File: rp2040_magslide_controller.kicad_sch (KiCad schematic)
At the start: 45 parts, among them J1 USB_B_Mini, J2 50-00174, J3 Conn_02x05_Odd_Even, J4 Conn_01x20_Female, J5 Conn_01x20_Female, SW2 SW_SPST, U2 AMS1117-3.3, U4 CD74HC4067SM, U5 CD74HC4067SM

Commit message: Inc
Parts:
- added C20: 0.1u, symbol Device:C_Small
- added H1: (no value), symbol Mechanical:MountingHole
- added H2, H3, H4: MountingHole, symbol Mechanical:MountingHole
- C1, C10, C11, C12, C13, C14, C15, C16, C17: value (none) -> 0.1u
- C4, C5: value (none) -> 12p
- C9: value 0.1u -> (none)
- R2: value (none) -> 1K
- R4: value (none) -> 10K
- R8: value (none) -> 27R 0603
- SW1: value (none) -> SW_SPST
- U1: value (none) -> W25Q64JV; footprint (none) -> Package_SON:WSON-8-1EP_6x5mm_P1.27mm_EP3.4x4mm
- U3: value (none) -> RP2040; footprint (none) -> RP2040_minimal:RP2040-QFN-56
- Y1: value (none) -> 12Mhz
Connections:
- net +3V3: now also C11.1, C12.1, C13.1, C14.1, C15.1, C16.1, C17.1, C20.1; no longer C11.2, C12.2, C13.2, C14.2, C15.2, C16.2, C17.2
- net GND: now also C10.2, C11.2, C12.2, C13.2, C14.2, C15.2, C16.2, C17.2, C8.2, C9.2, C20.2; no longer C10.1, C11.1, C12.1, C13.1, C14.1, C15.1, C16.1, C17.1, C8.1, C9.1
- net +1V1: now reaches U3.23 (DVDD), U3.45 (VREG_VOUT), U3.50 (DVDD)
- net +1V1: now also C10.1, C8.1, C9.1; no longer C10.2, C8.2, C9.2
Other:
- note added: "Close to chip"
- moved on the sheet: C2, C3, C6, C7, U2

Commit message: WIP for layout, need new footprint for rp2040 for some reason...
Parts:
- removed J4, J5: Conn_01x20_Female, misc:20_pin_header, symbol Connector:Conn_01x20_Female
- added J4: (no value), symbol Connector_Generic:Conn_02x20_Odd_Even
- C8: value (none) -> 0.1u
- C9: value (none) -> 1u
- H1: value (none) -> MountingHole
- U3: footprint RP2040_minimal:RP2040-QFN-56 -> (none)
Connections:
- net +3V3: now also J4.1 (Pin_1), J4.15 (Pin_15), J4.18 (Pin_18), J4.29 (Pin_29), J4.4 (Pin_4)
- net +5V: now also J4.36 (Pin_36)
- net F00: now also J4.5 (Pin_5)
- net F01: now also J4.7 (Pin_7)
- net F02: now also J4.9 (Pin_9)
- net F03: now also J4.11 (Pin_11)
- net F04: now also J4.13 (Pin_13)
- net F10: now also J4.19 (Pin_19)
- net F11: now also J4.21 (Pin_21)
- net F12: now also J4.23 (Pin_23)
- net F13: now also J4.25 (Pin_25)
- net F14: now also J4.27 (Pin_27)
- net F20: now also J4.33 (Pin_33)
- net F21: now also J4.35 (Pin_35)
- net F22: now also J4.37 (Pin_37)
- net F23: now also J4.39 (Pin_39)
- net F24: now also J4.2 (Pin_2)
- net F30: now also J4.8 (Pin_8)
- net F31: now also J4.10 (Pin_10)
- net F32: now also J4.12 (Pin_12)
- net F33: now also J4.14 (Pin_14)
- net F34: now also J4.16 (Pin_16)
- net F40: now also J4.22 (Pin_22)
- net F41: now also J4.24 (Pin_24)
- net F42: now also J4.26 (Pin_26)
- net F43: now also J4.28 (Pin_28)
- net F44: now also J4.30 (Pin_30)
- net GND: now also J4.17 (Pin_17), J4.20 (Pin_20), J4.3 (Pin_3), J4.31 (Pin_31), J4.38 (Pin_38), J4.6 (Pin_6)
- net extern_scl: now also J4.32 (Pin_32)
- net extern_sda: now also J4.34 (Pin_34)

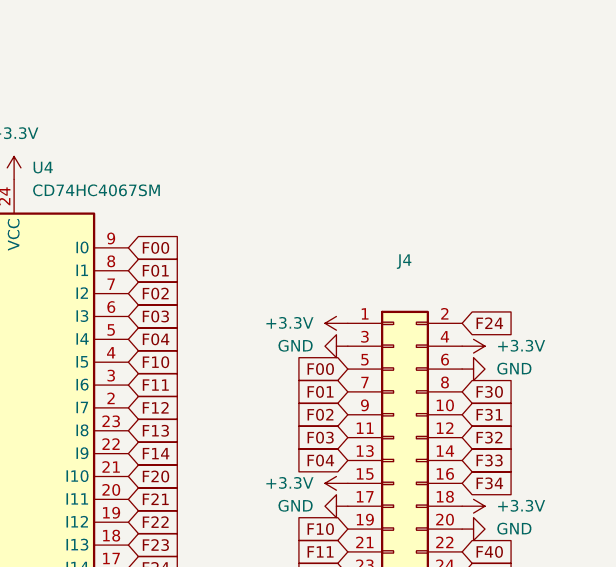
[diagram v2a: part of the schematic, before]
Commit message: Adds SOP8 flash instead
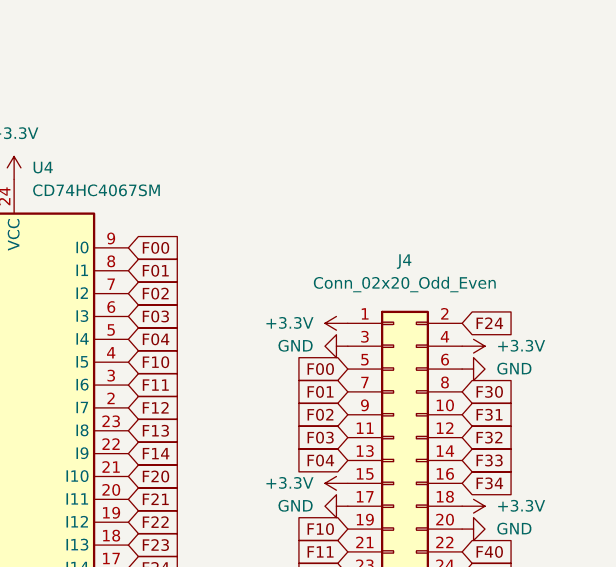
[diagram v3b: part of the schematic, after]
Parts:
- C1, C10, C11, C12, C13, C14, C15, C16, C17, C20, C4, C5, C8: footprint (none) -> Capacitor_SMD:C_0402_1005Metric
- C9: footprint (none) -> Capacitor_SMD:C_0603_1608Metric
- H1, H2, H3, H4: footprint (none) -> MountingHole:MountingHole_3.2mm_M3
- J4: value (none) -> Conn_02x20_Odd_Even; footprint (none) -> Connector_PinSocket_2.54mm:PinSocket_2x20_P2.54mm_Vertical
- R2, R4, R7: footprint (none) -> Resistor_SMD:R_0402_1005Metric
- R8, R9: footprint (none) -> Resistor_SMD:R_0603_1608Metric
- SW1, SW2: footprint (none) -> local:SW_TS-1187A-B-A-B
- U1: footprint Package_SON:WSON-8-1EP_6x5mm_P1.27mm_EP3.4x4mm -> (none)
- U3: footprint (none) -> MCU_RaspberryPi_and_Boards:RP2040-QFN-56
- Y1: footprint (none) -> Crystal:Crystal_SMD_3225-4Pin_3.2x2.5mm
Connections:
- net GND: no longer U1.9 (GND)

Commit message: Inc
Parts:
- removed C18, C19: 100n, Capacitor_SMD:C_0402_1005Metric, symbol Device:C_Small
- removed C2, C6: 4u7, Capacitor_SMD:C_0603_1608Metric, symbol Device:C_Small
- removed C3, C7: 1u, Capacitor_SMD:C_0603_1608Metric, symbol Device:C_Small
- removed H1, H2, H3, H4: MountingHole, MountingHole:MountingHole_3.2mm_M3, symbol Mechanical:MountingHole
- removed J1: USB_B_Mini, Connector_USB:USB_Micro-B_Molex-105017-0001, symbol Connector:USB_B_Mini
- removed J4: Conn_02x20_Odd_Even, Connector_PinSocket_2.54mm:PinSocket_2x20_P2.54mm_Vertical, symbol Connector_Generic:Conn_02x20_Odd_Even
- removed JP1, JP2: SolderJumper_2_Open, Jumper:SolderJumper-2_P1.3mm_Open_TrianglePad1.0x1.5mm, symbol Jumper:SolderJumper_2_Open
- removed R10, R11: 10k, Resistor_SMD:R_0402_1005Metric, symbol Device:R_Small
- removed R2: 1K, Resistor_SMD:R_0402_1005Metric, symbol Device:R_Small
- removed R5, R6: 4.7k, Resistor_SMD:R_0402_1005Metric, symbol Device:R_Small
- removed R8, R9: 27R 0603, Resistor_SMD:R_0603_1608Metric, symbol Device:R_Small
- removed SW1, SW2: SW_SPST, local:SW_TS-1187A-B-A-B, symbol Switch:SW_SPST
- removed U2: AMS1117-3.3, Package_TO_SOT_SMD:SOT-223-3_TabPin2, symbol Regulator_Linear:AMS1117-3.3
- removed U4, U5: CD74HC4067SM, Package_SO:SSOP-24_5.3x8.2mm_P0.65mm, symbol 74xx:CD74HC4067SM
- added C? (x3): 10uF, Capacitor_SMD:C_0603_1608Metric, symbol Device:C_Small
- added C?: 100nF, Capacitor_SMD:C_0603_1608Metric, symbol Device:C_Small
- added J?: Pressure sensor, symbol Connector:Conn_01x02_Female
- added JP? (x3): SolderJumper_2_Open, symbol Jumper:SolderJumper_2_Open
- added R?: 10k, Resistor_SMD:R_0402_1005Metric, symbol Device:R_Small
- added S? (x4): OH49E-S, symbol magslide:OH49E-S
- added U?: AP2112K-3.3, Package_TO_SOT_SMD:SOT-23-5, symbol Regulator_Linear:AP2112K-3.3
- added U?: LIS3DH, Package_LGA:LGA-16_3x3mm_P0.5mm_LayoutBorder3x5y, symbol Sensor_Motion:LIS3DH
- added U?: SGM3157, symbol magslide:SGM3157
- U1: footprint (none) -> Package_SO:SOP-8_5.28x5.23mm_P1.27mm
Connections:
- net +3V3: now also C?.1, C?.1, J?.1 (Pin_1), S?.1 (VCC), S?.1 (VCC), S?.1 (VCC), S?.1 (VCC), U?.5 (VOUT), U?.5 (Vcc)
- net +5V: now also C?.1, C?.1, U?.1 (VIN), U?.3 (EN)
- net GND: now also C?.2, C?.2, C?.2, C?.2, R?.1, S?.3 (GND), S?.3 (GND), S?.3 (GND), S?.3 (GND), U?.2 (GND), U?.2 (Gnd)
- net board_scl: now also R1.2
- net board_sda: now also R3.2
- net SENS3: now reaches U3.40 (GPIO28_ADC2)
- net SENS3: now also S?.2 (OUT)
- net ADC4: now reaches U3.41 (GPIO29_ADC3)
- net ADC4: now also JP?.2 (B), JP?.2 (B)
- net ADC_0 renamed SENS1
- net SENS1: now also S?.2 (OUT)
- net ADC_1 renamed SENS2
- net SENS2: now also S?.2 (OUT)
- net MUX0_EN: no longer names the net of U3.8 (GPIO6)
- net MUX1_EN: no longer names the net of U3.14 (GPIO11)
- net MUX_00: no longer names the net of U3.9 (GPIO7)
- net MUX_01: no longer names the net of U3.11 (GPIO8)
- net MUX_02: no longer names the net of U3.12 (GPIO9)
- net MUX_03 renamed ADC4_SEL
- net ADC4_SEL: now also U?.6 (Select)
- net MUX_10: no longer names the net of U3.15 (GPIO12)
- net MUX_11: no longer names the net of U3.16 (GPIO13)
- net MUX_12: no longer names the net of U3.17 (GPIO14)
- net MUX_13: no longer names the net of U3.18 (GPIO15)
- net extern_scl: no longer names the net of U3.5 (GPIO3)
- net extern_sda: no longer names the net of U3.4 (GPIO2)
- new net: JP?.1 (A), U?.4 (A)
- new net: U?.10 (GND), U?.12 (GND), U?.5 (GND)
- new net: JP?.2 (B), U?.3 (B0)
- new net PRESSURE: J?.2 (Pin_2), R?.2, U?.1 (B1)
- new net SENS4: JP?.1 (A), JP?.1 (A), S?.2 (OUT)
- no-connect marks 23 -> 14
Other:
- note removed: "Close to chip"
- moved on the sheet: R4, R7

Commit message: Inc
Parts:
- removed JP? (x2): SolderJumper_2_Open, symbol Jumper:SolderJumper_2_Open
- added C?: 10uF, Capacitor_SMD:C_0603_1608Metric, symbol Device:C_Small
- added C?: 100nF, Capacitor_SMD:C_0603_1608Metric, symbol Device:C_Small
- added JP?: SolderJumper_3_Open, symbol Jumper:SolderJumper_3_Open
- added R? (x2): 10k, Resistor_SMD:R_0402_1005Metric, symbol Device:R_Small
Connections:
- net +3V3: now also U?.1 (VDD_IO), U?.14 (VDD), U?.8 (CS), C?.1, C?.1, R?.1, R?.1
- net ADC4: now also JP?.2 (C)
- net GND: now also U?.10 (GND), U?.12 (GND), U?.5 (GND), U?.7 (SDO/SA0), C?.2, C?.2
- net SENS4: now also JP?.1 (A)
- net at U3.4 (GPIO2): now also U?.6 (SDA/SDI/SDO), R?.2
- net at U3.5 (GPIO3): now also U?.4 (SCL/SPC), R?.2
- net MUX_OUT: now reaches U?.4 (A)
- net MUX_OUT: now also JP?.3 (B)
- no-connect marks 14 -> 19
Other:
- moved on the sheet: U?

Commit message: Inc
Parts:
- J1: renamed from J?; footprint (none) -> Connector_PinHeader_1.00mm:PinHeader_1x02_P1.00mm_Vertical
- JP1: renamed from JP?; footprint (none) -> Jumper:SolderJumper-2_P1.3mm_Open_RoundedPad1.0x1.5mm
- JP2: renamed from JP?; footprint (none) -> Jumper:SolderJumper-3_P1.3mm_Open_RoundedPad1.0x1.5mm
- S1, S2, S3, S4: renamed from S?; footprint (none) -> Package_TO_SOT_SMD:SOT-23
- U5: renamed from U?; footprint (none) -> misc:SC70-6
- gave numbers to parts that had none: 11
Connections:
- no-connect marks 19 -> 28

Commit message: WIP
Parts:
- removed C3: 10uF, Capacitor_SMD:C_0603_1608Metric, symbol Device:C_Small
- removed C6: 100nF, Capacitor_SMD:C_0603_1608Metric, symbol Device:C_Small
- removed R1, R3: 4.7k, Resistor_SMD:R_0402_1005Metric, symbol Device:R_Small

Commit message: Updated JLCPCB
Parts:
- C18: footprint Capacitor_SMD:C_0603_1608Metric -> Capacitor_SMD:C_0402_1005Metric
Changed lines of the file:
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@@
       (effects (font (size 1.27 1.27)) (justify left))
     )
-    (property "Footprint" "Capacitor_SMD:C_0603_1608Metric" (id 2) (at 205.74 33.02 0)
+    (property "Footprint" "Capacitor_SMD:C_0402_1005Metric" (id 2) (at 205.74 33.02 0)
       (effects (font (size 1.27 1.27)) hide)
     )
@@
     )
     (path "/cc9cebe2-9d12-4fc5-bd7f-48e9932ba62c"
-      (reference "C18") (unit 1) (value "100nF") (footprint "Capacitor_SMD:C_0603_1608Metric")
+      (reference "C18") (unit 1) (value "100nF") (footprint "Capacitor_SMD:C_0402_1005Metric")
     )
     (path "/10913d2a-ae41-45bd-87e4-e0e08e2ac266"
